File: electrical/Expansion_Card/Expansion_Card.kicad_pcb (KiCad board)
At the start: 4 copper layers, 29.3 x 30 mm, 38 parts, among them J1 Micro_SD_Card_Det2, J2 SD_Card_Receptacle, P1 USB_C_Plug_USB2.0, U1 AP2112K-3.3, U2 USB2660I-JZX-03, X1 24MHz ASCO

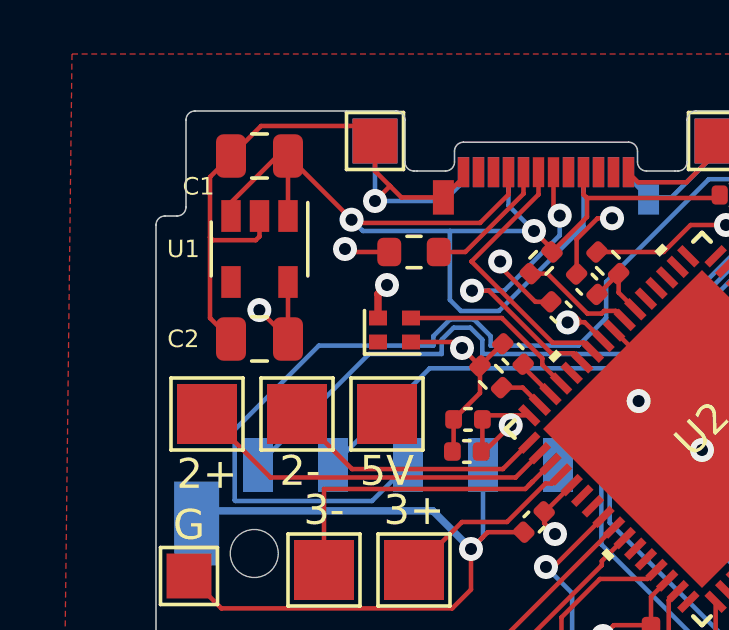
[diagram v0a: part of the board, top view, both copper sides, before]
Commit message: finish routing USB pads for Rev2
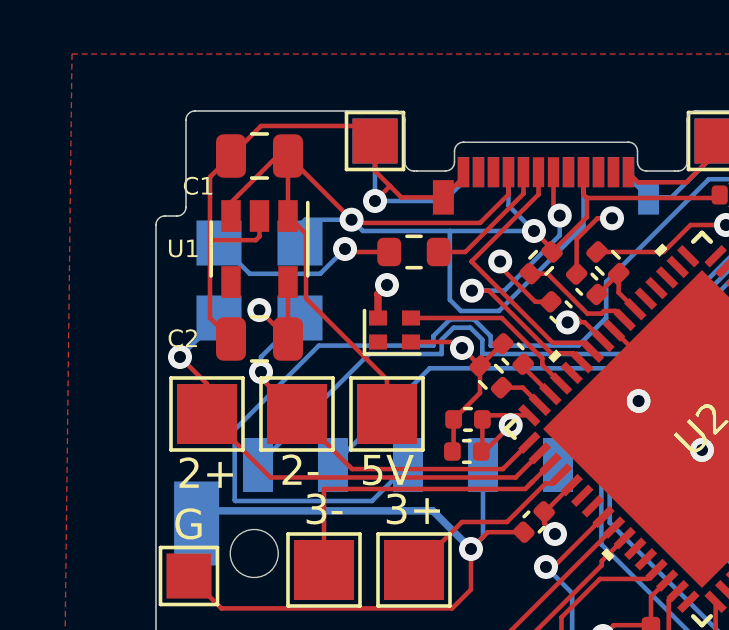
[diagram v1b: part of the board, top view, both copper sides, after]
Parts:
- added 2+: TestPoint_Pad_1.5x1.5mm, TestPoint:TestPoint_Pad_1.5x1.5mm, B.Cu at (129.1, 133.9)
- added 2-: TestPoint_Pad_1.5x1.5mm, TestPoint:TestPoint_Pad_1.5x1.5mm, B.Cu at (131.8, 133.9)
- added 5V: TestPoint_Pad_1.5x1.5mm, TestPoint:TestPoint_Pad_1.5x1.5mm, B.Cu at (131.8, 131.4)
- added G: TestPoint_Pad_1.5x1.5mm, TestPoint:TestPoint_Pad_1.5x1.5mm, B.Cu at (129.1, 131.4)
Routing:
- net VBUS: track 41.4 -> 52.0 mm
- net GND: track 125.7 -> 130.7 mm
- net Net-(U2-USBDN_DM2): track 8.87 -> 13.1 mm, vias 0 -> 1
- net Net-(U2-USBDN_DP2): track 12.3 -> 16.4 mm, vias 0 -> 1

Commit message: I have regrets
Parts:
- removed 2+, 2-: TestPoint, TestPoint:TestPoint_Pad_2.0x2.0mm
- removed 2+, 2-: TestPoint_Pad_1.5x1.5mm, TestPoint:TestPoint_Pad_1.5x1.5mm
- removed 3+: 3-, TestPoint:TestPoint_Pad_2.0x2.0mm
- removed 3-: 3+, TestPoint:TestPoint_Pad_2.0x2.0mm
- removed the 5V at (134.7, 137.1)
- removed the G at (128.1, 142.5)
- added IC1: GL823K, Expansion_Card:SOP64P600X175-16N, F.Cu at (133.7, 139.4)
- added J3: Micro_SD_Card_Det2, Connector_Card:microSD_HC_Molex_104031-0811, F.Cu at (147.5, 151.0)
- moved C4 4.64 mm to (152.5, 143.4), turned to 0 degrees
- moved C6 3.05 mm to (140.8, 143.3), turned to 180 degrees
- moved C15 2.34 mm to (142.8, 143.9), turned to 180 degrees
- moved C7 0.71 mm to (150.3, 142.4)
- moved C8 0.71 mm to (149.5, 143.2)
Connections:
- U2 pad 1: Net-(U2-USBDN_DM2) -> /U2-
- U2 pad 2: Net-(U2-USBDN_DP2) -> /U2+
- U2 pad 3: Net-(U2-USBDN_DM3) -> unconnected-(U2-USBDN_DM3-Pad3)
- U2 pad 4: Net-(U2-USBDN_DP3) -> unconnected-(U2-USBDN_DP3-Pad4)
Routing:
- net unconnected-(J3-SHIELD-Pad11): track 0.00 -> 33.5 mm, vias 0 -> 4
- net Net-(IC1-D3): track 0.00 -> 29.9 mm, vias 0 -> 2
- net Net-(IC1-CLK): track 0.00 -> 27.9 mm, vias 0 -> 2
- net Net-(IC1-D0): track 0.00 -> 26.5 mm, vias 0 -> 2
- net Net-(IC1-CMD): track 0.00 -> 26.5 mm, vias 0 -> 2
- net /U2-: track 0.00 -> 24.0 mm, vias 0 -> 2
- net Net-(IC1-D2): track 0.00 -> 23.3 mm, vias 0 -> 2
- net /uSD2-pwr: track 0.00 -> 19.0 mm, vias 0 -> 2
- net Net-(U2-USBDN_DP2): track 16.4 -> 0.00 mm, vias 1 -> 0
- net unconnected-(J1-SHIELD-Pad11): track 21.7 -> 35.6 mm, vias 2 -> 4
- net Net-(U2-USBDN_DM2): track 13.1 -> 0.00 mm, vias 1 -> 0
- net Net-(U2-USBDN_DM3): track 10.8 -> 0.00 mm
- net /U2+: track 0.00 -> 10.3 mm
- net +3V3: track 39.4 -> 47.5 mm
- net GND: track 130.7 -> 138.5 mm, vias 15 -> 18
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
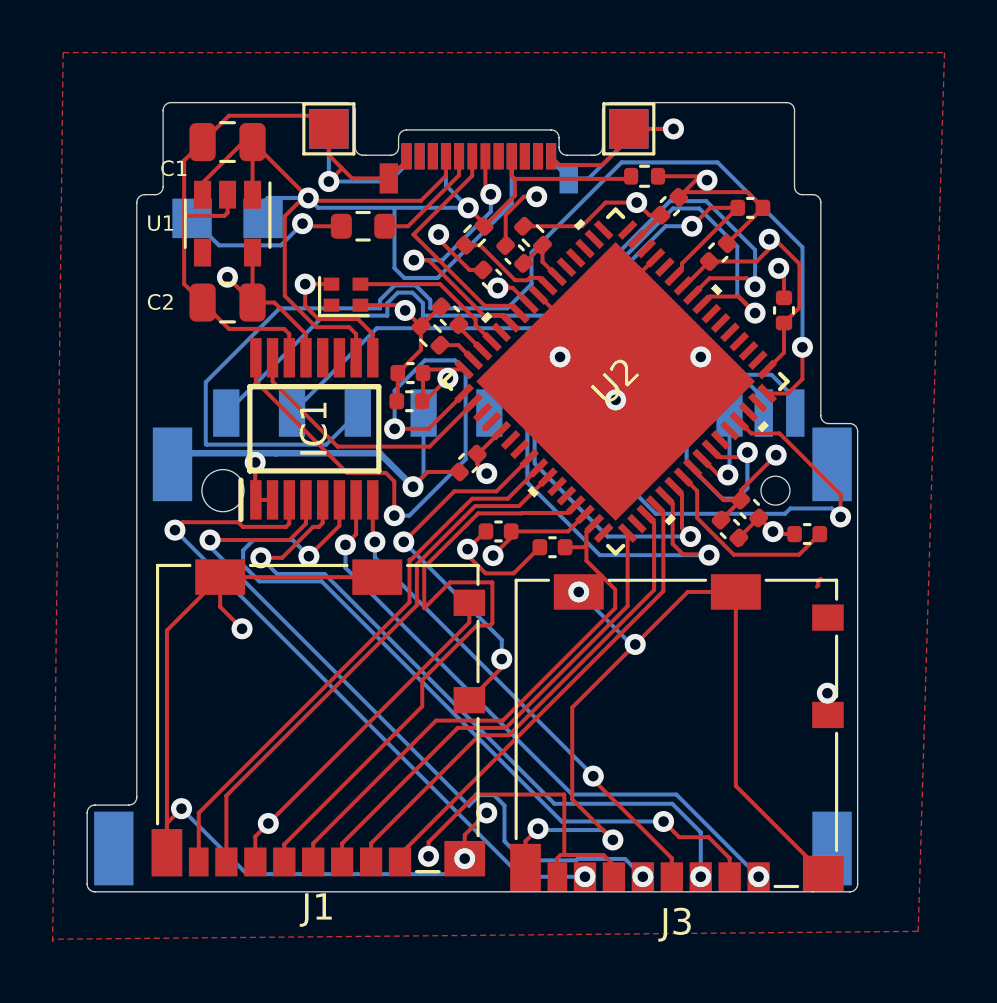
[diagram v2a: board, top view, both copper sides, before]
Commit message: restore pads to access 2nd downstream USB2.0 on the backside
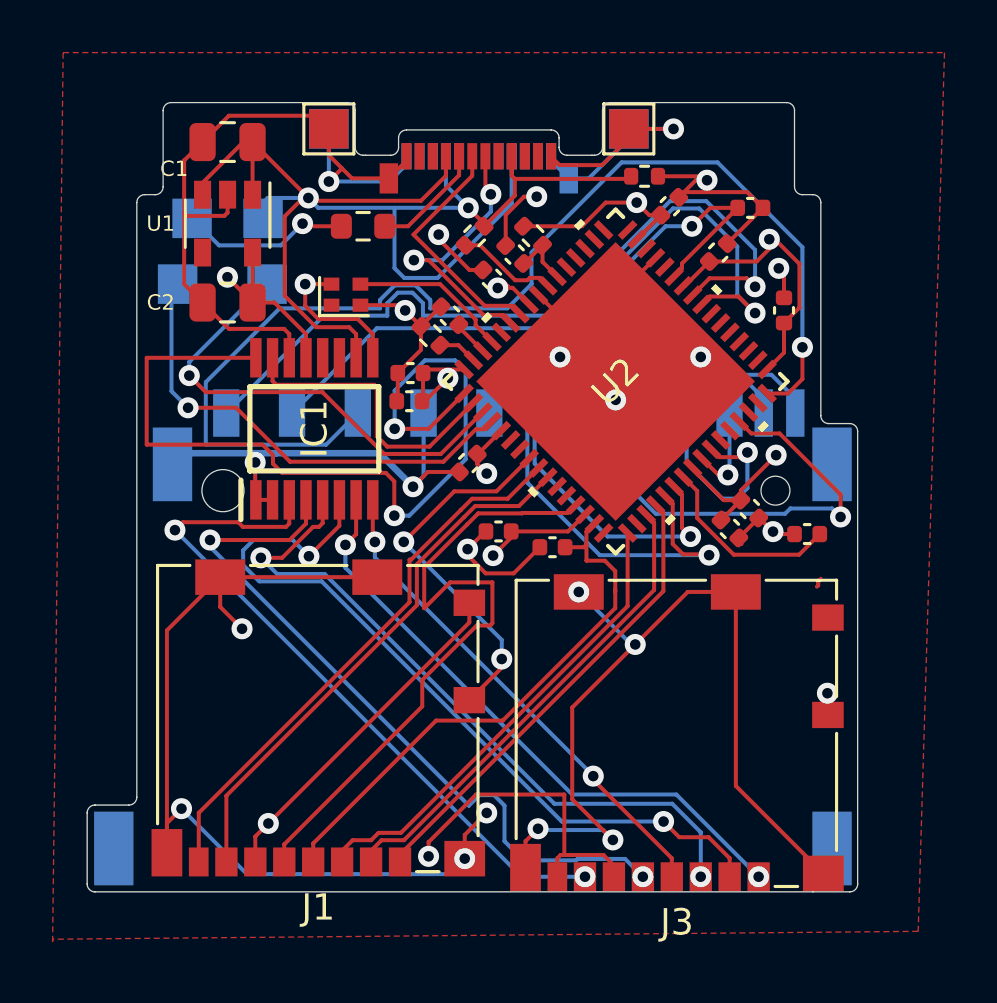
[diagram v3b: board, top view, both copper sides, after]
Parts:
- added D+: TestPoint_Pad_1.5x1.5mm, TestPoint:TestPoint_Pad_1.5x1.5mm, B.Cu at (128.6, 133.9)
- added D-: TestPoint_Pad_1.5x1.5mm, TestPoint:TestPoint_Pad_1.5x1.5mm, B.Cu at (131.9, 133.9)
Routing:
- net unconnected-(U2-USBDN_DM3-Pad3): track 0.00 -> 17.7 mm, vias 0 -> 1
- net unconnected-(U2-USBDN_DP3-Pad4): track 0.42 -> 18.1 mm, vias 0 -> 1
- net /U2-: track 24.0 -> 33.9 mm
- net /U2+: track 10.3 -> 11.3 mm
- net Net-(J1-VDD): track 20.5 -> 21.0 mm
